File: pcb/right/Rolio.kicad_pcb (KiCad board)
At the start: 2 copper layers, 141.8 x 83.9 mm, 110 parts, among them Q1 AO3400A, SW4 SW_DIP_x01

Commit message: Check in V1.0
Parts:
- H2: moved to B.Cu
- moved R3 2.03 mm to (85.3, 41.9)
- moved R5 1.20 mm to (121.4, 36.8)
- moved SW4 0.86 mm to (75.0, 41.6)
- moved BATT1 0.81 mm to (75.7, 48.3)
- moved C1 0.81 mm to (59.0, 80.6)
- moved C2 0.81 mm to (58.9, 85.6)
- moved Nice!View1 0.81 mm to (64.5, 74.1)
- moved RE_1 0.81 mm to (59.3, 84.1)
- moved NICE_NANO1 0.81 mm to (51.8, 41.0)
- moved RESET1 0.81 mm to (71.9, 50.4)
- moved D19 0.81 mm to (59.2, 91.2)
- moved D1 0.53 mm to (80.3, 45.3)
- turned H2 to 180 degrees
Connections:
- SW4 pad 1: Net-(BATT1-+) -> (no net)
- SW4 pad 3: (no net) -> Net-(BATT1-+)
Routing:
- net row0: track 168.9 -> 160.2 mm
- net Net-(D1-A): track 8.79 -> 16.7 mm
- net Net-(BATT1-+): track 4.80 -> 12.1 mm
- net col5: track 76.0 -> 82.2 mm
- net BL_GND: track 523.9 -> 521.1 mm
- net GND: track 91.8 -> 89.0 mm, vias 15 -> 16
- net row3: track 143.6 -> 141.5 mm
- net col1: track 204.5 -> 203.6 mm
- net Net-(D19-A): track 26.7 -> 25.8 mm
- net BL_CTRL: track 177.4 -> 178.2 mm
- net row2: track 187.8 -> 188.5 mm
- net col0: track 204.5 -> 203.8 mm
- net VCC: track 562.6 -> 562.0 mm
- net CS: track 83.7 -> 84.2 mm
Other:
- board size 141.8 x 83.9 mm -> 141.5 x 83 mm
- board text added: "+"
- board text added: "Rolio V1.2 (Right) - MickiusMousius '23"
- board text removed: "Rolio V1.01 (Right) - MickiusMousius '23"

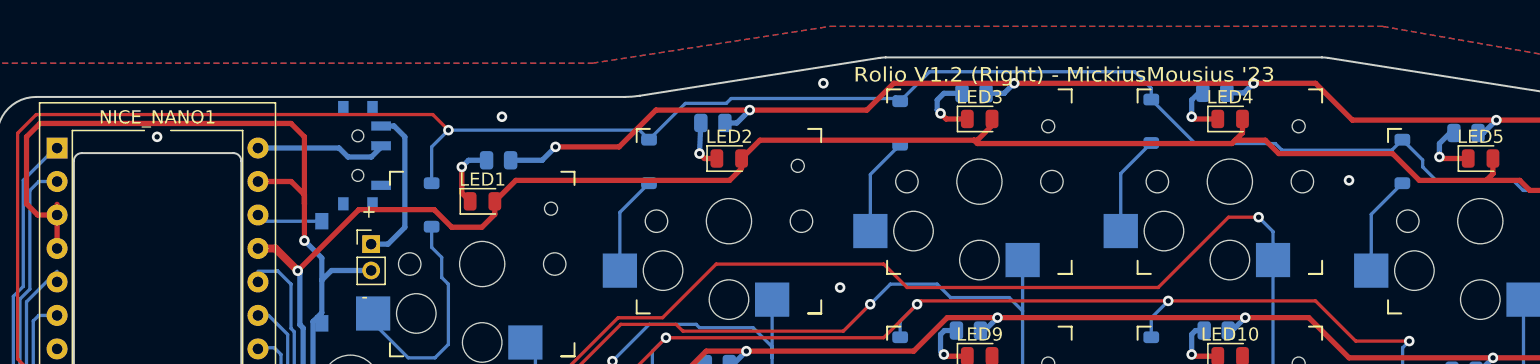
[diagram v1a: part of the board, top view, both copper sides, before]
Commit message: Update the right PCB to have a nicer set of solder pads for the battery
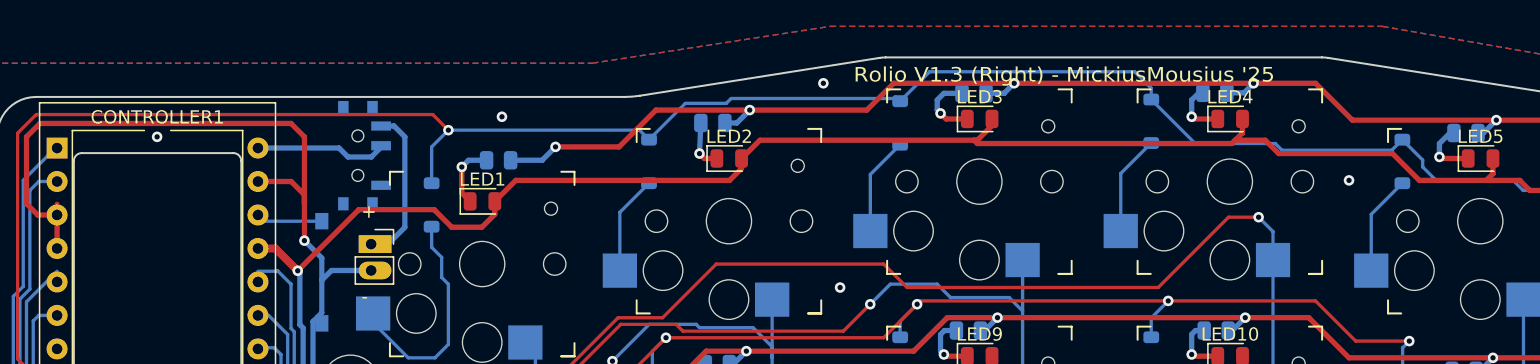
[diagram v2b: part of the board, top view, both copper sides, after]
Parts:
- renumbered NICE_NANO1 to CONTROLLER1
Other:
- board text added: "Rolio V1.3 (Right) - MickiusMousius '25"
- board text removed: "Rolio V1.2 (Right) - MickiusMousius '23"
